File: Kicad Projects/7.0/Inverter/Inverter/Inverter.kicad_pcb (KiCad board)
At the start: 4 copper layers, 80.3 x 134.5 mm, 107 parts, among them IC1 1ED3322MC12NXUMA1, IC2 B0505S-2W, IC3 B0505S-2W, IC4 B0505S-2W, IC5 1ED3322MC12NXUMA1, J1 Conn_01x02_Male, J2 Conn_01x07_Male, J3 Conn_01x02_Male, J4 Output Selector, J5 Conn_01x07_Male, J6 Conn_01x03_Pin, J7 Conn_01x03_Pin, Q1 FS8205, Q2 FS8205, U1 LM7809_TO220, U2 LM7809_TO220, U3 LM7809_TO220, U4 AMS1117-5.0, U5 AMS1117-5.0, U6 AMS1117-5.0, U7 FF300R12KS4, U8 AMS1117-3.3, U9 ChinaBluePill

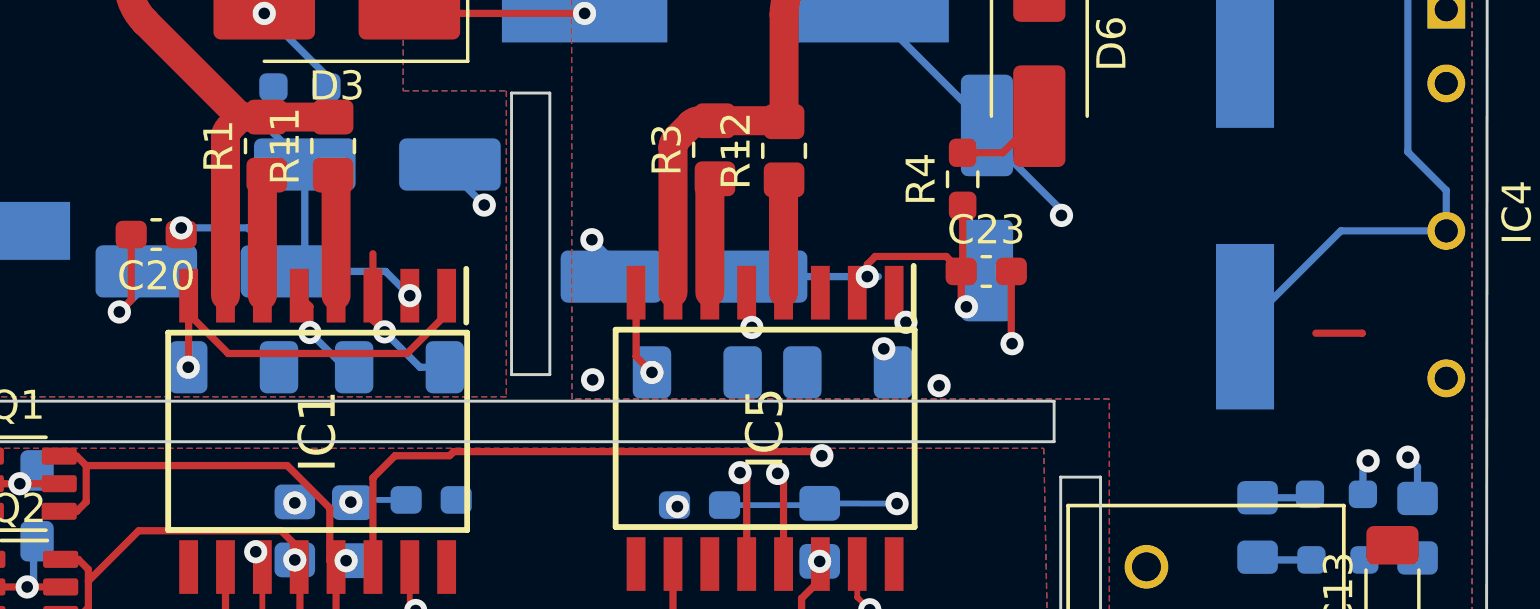
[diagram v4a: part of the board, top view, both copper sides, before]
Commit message: Inverter changes - power routing - incomplete
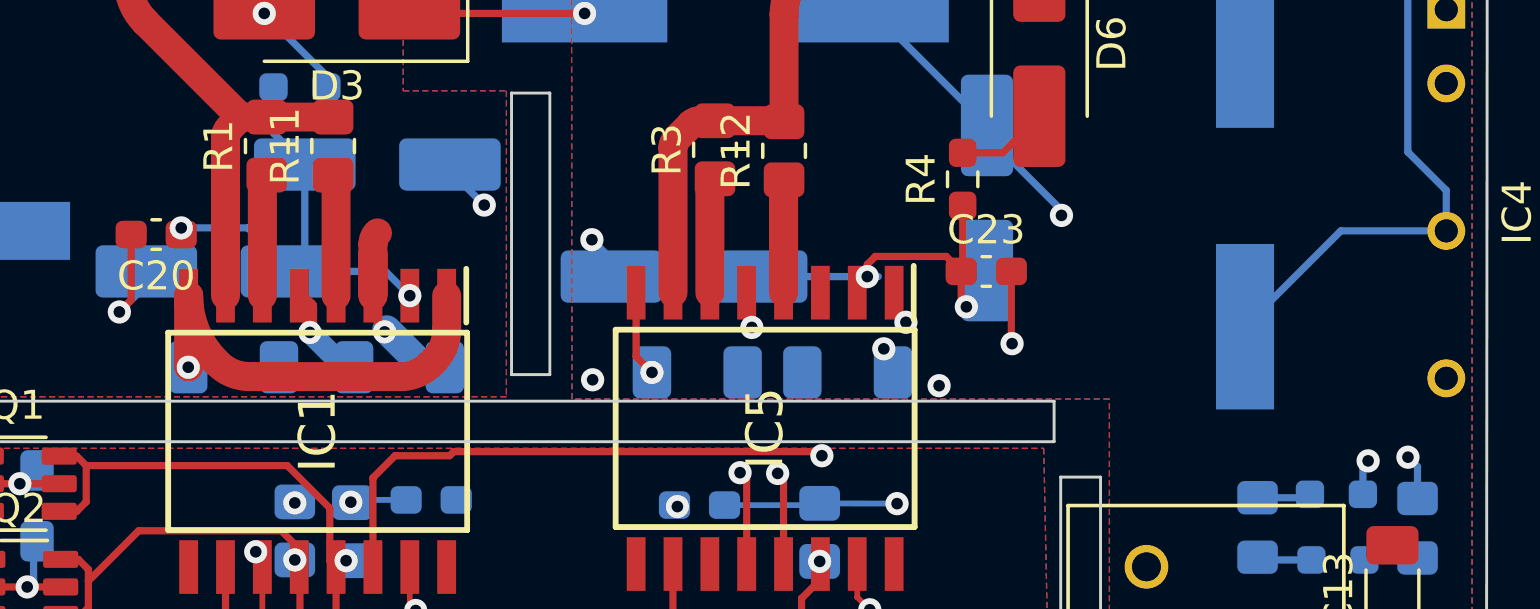
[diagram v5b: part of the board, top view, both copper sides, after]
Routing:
- net GND1: track 7.37 -> 11.9 mm
- net VDrive1Neg: track 23.4 -> 25.4 mm
- net GND2: track 11.4 -> 9.84 mm
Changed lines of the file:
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@@
   (segment (start 48.1584 155.9175) (end 50.9139 155.9175) (width 0.25) (layer "B.Cu") (net 5))
   (segment (start 25.908 130.302) (end 26.035 130.429) (width 0.25) (layer "F.Cu") (net 6))
-  (segment (start 52.920645 134.680445) (end 52.5526 134.3124) (width 0.25) (layer "F.Cu") (net 6))
+  (segment (start 52.920645 134.680445) (end 52.5526 134.3124) (width 0.5) (layer "F.Cu") (net 6))
   (segment (start 52.5526 134.3124) (end 52.5526 134.8871) (width 0.25) (layer "F.Cu") (net 6))
-  (segment (start 52.920645 135.580944) (end 52.920645 134.680445) (width 0.25) (layer "F.Cu") (net 6))
+  (segment (start 52.920645 135.580944) (end 52.920645 134.680445) (width 0.5) (layer "F.Cu") (net 6))
   (segment (start 23.622 130.302) (end 25.908 130.302) (width 0.25) (layer "F.Cu") (net 6))
   (segment (start 37.75588 135.03788) (end 37.973 135.255) (width 0.25) (layer "F.Cu") (net 6))
@@
   (via (at 37.973 135.255) (size 0.8) (drill 0.4) (layers "F.Cu" "B.Cu") (net 6))
   (via (at 26.035 130.429) (size 0.8) (drill 0.4) (layers "F.Cu" "B.Cu") (net 6))
-  (segment (start 54.118701 136.779) (end 52.920645 135.580944) (width 0.25) (layer "B.Cu") (net 6))
+  (segment (start 52.920645 135.580944) (end 54.118701 136.779) (width 0.75) (layer "B.Cu") (net 6))
   (segment (start 19.837 137.019) (end 19.587 137.019) (width 0.25) (layer "B.Cu") (net 6))
   (segment (start 18.2195 139.8955) (end 16.365 139.8955) (width 0.25) (layer "B.Cu") (net 6))
@@
   (segment (start 54.4445 136.779) (end 54.118701 136.779) (width 0.25) (layer "B.Cu") (net 6))
   (segment (start 35.7995 131.69) (end 35.9175 131.572) (width 0.25) (layer "F.Cu") (net 7))
-  (segment (start 55.0926 134.3124) (end 55.0926 132.8674) (width 0.25) (layer "F.Cu") (net 7))
-  (segment (start 55.0926 135.159102) (end 55.494201 135.560703) (width 0.25) (layer "F.Cu") (net 7))
+  (segment (start 55.0926 134.3124) (end 55.0926 132.8674) (width 1) (layer "F.Cu") (net 7))
+  (segment (start 55.0926 134.3124) (end 55.0926 132.529997) (width 1) (layer "F.Cu") (net 7))
+  (segment (start 55.0926 134.3124) (end 55.0926 134.591153) (width 0.25) (layer "F.Cu") (net 7))
   (segment (start 34.036 131.69) (end 35.7995 131.69) (width 0.25) (layer "F.Cu") (net 7))
-  (segment (start 55.0926 134.3124) (end 55.0926 135.159102) (width 0.25) (layer "F.Cu") (net 7))
   (via (at 55.494201 135.560703) (size 0.8) (drill 0.4) (layers "F.Cu" "B.Cu") (net 7))
-  (segment (start 56.712498 136.779) (end 57.5695 136.779) (width 0.25) (layer "B.Cu") (net 7))
-  (segment (start 55.494201 135.560703) (end 56.712498 136.779) (width 0.25) (layer "B.Cu") (net 7))
+  (arc (start 55.0926 134.591153) (mid 55.196972 135.115869) (end 55.494201 135.560703) (width 0.25) (layer "F.Cu") (net 7))
+  (arc (start 55.0926 132.529997) (mid 55.133507 132.324344) (end 55.25 132.15) (width 1) (layer "F.Cu") (net 7))
+  (segment (start 55.494201 135.560703) (end 56.106506 136.173008) (width 0.25) (layer "B.Cu") (net 7))
+  (segment (start 57.5695 136.779) (end 56.85743 136.779) (width 1) (layer "B.Cu") (net 7))
+  (segment (start 56.85743 136.779) (end 55.566667 135.488237) (width 1) (layer "B.Cu") (net 7))
+  (arc (start 56.106506 136.173008) (mid 56.777733 136.621508) (end 57.5695 136.779) (width 0.25) (layer "B.Cu") (net 7))
   (segment (start 90.1954 151.3463) (end 91.6309 151.3463) (width 0.25) (layer "F.Cu") (net 8))
   (segment (start 91.6309 151.3463) (end 91.9988 151.7142) (width 0.25) (layer "F.Cu") (net 8))
@@
   (segment (start 76.2254 128.778) (end 78.8162 131.3688) (width 0.25) (layer "B.Cu") (net 8))
   (segment (start 56.348 124.587) (end 62.3852 124.587) (width 0.25) (layer "F.Cu") (net 9))
-  (segment (start 87.5806 135.6062) (end 89.175 135.6062) (width 0.25) (layer "F.Cu") (net 9))
-  (segment (start 89.175 135.6062) (end 89.1794 135.6106) (width 0.25) (layer "F.Cu") (net 9))
   (via (at 62.6618 137.2108) (size 0.8) (drill 0.4) (layers "F.Cu" "B.Cu") (free) (net 9))
   (via (at 74.5998 137.414) (size 0.8) (drill 0.4) (layers "F.Cu" "B.Cu") (free) (net 9))
@@
   (segment (start 54.4068 141.351) (end 54.3306 141.4272) (width 0.2) (layer "B.Cu") (net 15))
   (segment (start 37.9749 140.589) (end 37.0586 140.589) (width 0.2) (layer "B.Cu") (net 15))
-  (segment (start 48.7426 134.3124) (end 48.7426 136.7659) (width 0.25) (layer "F.Cu") (net 16))
+  (segment (start 57.6326 135.505612) (end 57.6326 134.3124) (width 1) (layer "F.Cu") (net 16))
+  (segment (start 48.7426 134.3124) (end 48.7426 136.7659) (width 1) (layer "F.Cu") (net 16))
   (segment (start 46.7625 134.4665) (end 46.355 134.874) (width 0.25) (layer "F.Cu") (net 16))
   (segment (start 39.624 133.74) (end 39.624 135.128) (width 0.25) (layer "F.Cu") (net 16))
-  (segment (start 56.269056 136.305944) (end 50.106144 136.305944) (width 0.25) (layer "F.Cu") (net 16))
   (segment (start 39.624 135.128) (end 39.497 135.255) (width 0.25) (layer "F.Cu") (net 16))
+  (segment (start 49.683193 136.583194) (end 49.75 136.65) (width 0.25) (layer "F.Cu") (net 16))
   (segment (start 46.7625 132.207) (end 46.7625 134.4665) (width 0.25) (layer "F.Cu") (net 16))
   (segment (start 48.7426 134.9424) (end 48.7426 134.3124) (width 0.25) (layer "F.Cu") (net 16))
-  (segment (start 57.6326 134.3124) (end 57.6326 134.9424) (width 0.25) (layer "F.Cu") (net 16))
-  (segment (start 57.6326 134.9424) (end 56.269056 136.305944) (width 0.25) (layer "F.Cu") (net 16))
   (segment (start 48.7426 136.7659) (end 48.7295 136.779) (width 0.25) (layer "F.Cu") (net 16))
-  (segment (start 50.106144 136.305944) (end 48.7426 134.9424) (width 0.25) (layer "F.Cu") (net 16))
+  (segment (start 50.836396 137.1) (end 56.05 137.1) (width 1) (layer "F.Cu") (net 16))
+  (segment (start 57.074264 136.675736) (end 57.2 136.55) (width 1) (layer "F.Cu") (net 16))
   (via (at 46.355 134.874) (size 0.8) (drill 0.4) (layers "F.Cu" "B.Cu") (net 16))
   (via (at 31.877 125.476) (size 0.8) (drill 0.4) (layers "F.Cu" "B.Cu") (net 16))
@@
   (via (at 39.497 135.255) (size 0.8) (drill 0.4) (layers "F.Cu" "B.Cu") (net 16))
   (via (at 31.877 130.302) (size 0.8) (drill 0.4) (layers "F.Cu" "B.Cu") (net 16))
+  (arc (start 48.7426 134.3124) (mid 48.987052 135.541345) (end 49.683193 136.583194) (width 1) (layer "F.Cu") (net 16))
+  (arc (start 56.05 137.1) (mid 56.604328 136.989737) (end 57.074264 136.675736) (width 1) (layer "F.Cu") (net 16))
+  (arc (start 49.75 136.65) (mid 50.248442 136.983049) (end 50.836396 137.1) (width 1) (layer "F.Cu") (net 16))
+  (arc (start 57.2 136.55) (mid 57.520171 136.070831) (end 57.6326 135.505612) (width 1) (layer "F.Cu") (net 16))
   (segment (start 47.284 133.477) (end 47.284 133.945) (width 0.25) (layer "B.Cu") (net 16))
   (segment (start 31.623 123.9905) (end 31.623 125.222) (width 0.25) (layer "B.Cu") (net 16))

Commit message: Inverter gbr generated
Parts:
- removed H1, H2, H3, H4: MountingHole, MountingHole:MountingHole_3.2mm_M3
- added J10: Conn_01x02_Pin, Connector_PinHeader_1.27mm:PinHeader_1x02_P1.27mm_Vertical, F.Cu at (84.0, 99.2)
- added J11: Conn_01x02_Pin, Connector_PinHeader_1.27mm:PinHeader_1x02_P1.27mm_Vertical, F.Cu at (87.5, 35.9)
- added J8: Conn_01x02_Pin, Connector_PinHeader_1.27mm:PinHeader_1x02_P1.27mm_Vertical, F.Cu at (88.4, 78.5)
- added J9: NTC, Connector_PinHeader_1.27mm:PinHeader_1x02_P1.27mm_Vertical, F.Cu at (49.0, 151.2)
- added R28: NTC Complement, Resistor_SMD:R_0805_2012Metric_Pad1.20x1.40mm_HandSolder, F.Cu at (49.6, 148.5)
- J2, J5: footprint Connector_JST:JST_XH_B7B-XH-A_1x07_P2.50mm_Vertical -> Connector_JST:JST_XH_B8B-XH-A_1x08_P2.50mm_Vertical
- moved J7 0.55 mm to (86.3, 31.8)
- moved J6 0.55 mm to (81.5, 107.8)
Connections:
- J6 pad 2: Net-(J6-Pin_2) -> Net-(J10-Pin_2)
- J7 pad 2: Net-(J6-Pin_2) -> Net-(J11-Pin_1)
- U9 pad PA0: unconnected-(U9-PadPA0) -> Net-(J8-Pin_1)
- U9 pad PA1: unconnected-(U9-PadPA1) -> Net-(J5-Pin_8)
- U9 pad PA12: Net-(J6-Pin_2) -> Net-(J10-Pin_1)
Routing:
- net Net-(J6-Pin_2): track 91.6 -> 0.00 mm, vias 1 -> 0
- net Net-(J10-Pin_1): track 0.00 -> 79.7 mm, vias 0 -> 1
- net /3V3 MCU: track 19.1 -> 65.6 mm, vias 4 -> 8
- net Net-(J5-Pin_8): track 0.00 -> 29.2 mm
- net Net-(J2-Pin_8): track 0.00 -> 28.3 mm
- net VDrive2Neg: track 31.2 -> 51.7 mm, vias 5 -> 6
- net GND2: track 9.84 -> 25.8 mm, vias 3 -> 4
- net GND1: track 11.9 -> 24.4 mm, vias 1 -> 2
- net Net-(J10-Pin_2): track 0.00 -> 7.28 mm
- net Net-(J11-Pin_1): track 0.00 -> 6.90 mm
- net VDrive2: track 17.1 -> 23.1 mm, vias 6 -> 8
- net Net-(IC5-CLAMP): track 20.2 -> 25.9 mm
- net Net-(J8-Pin_1): track 0.00 -> 3.51 mm
- net /OUTHS: track 0.00 -> 2.81 mm
- net INLS: track 33.3 -> 35.7 mm
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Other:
- outline, holes or cut-outs redrawn
- board text added: "NTC"

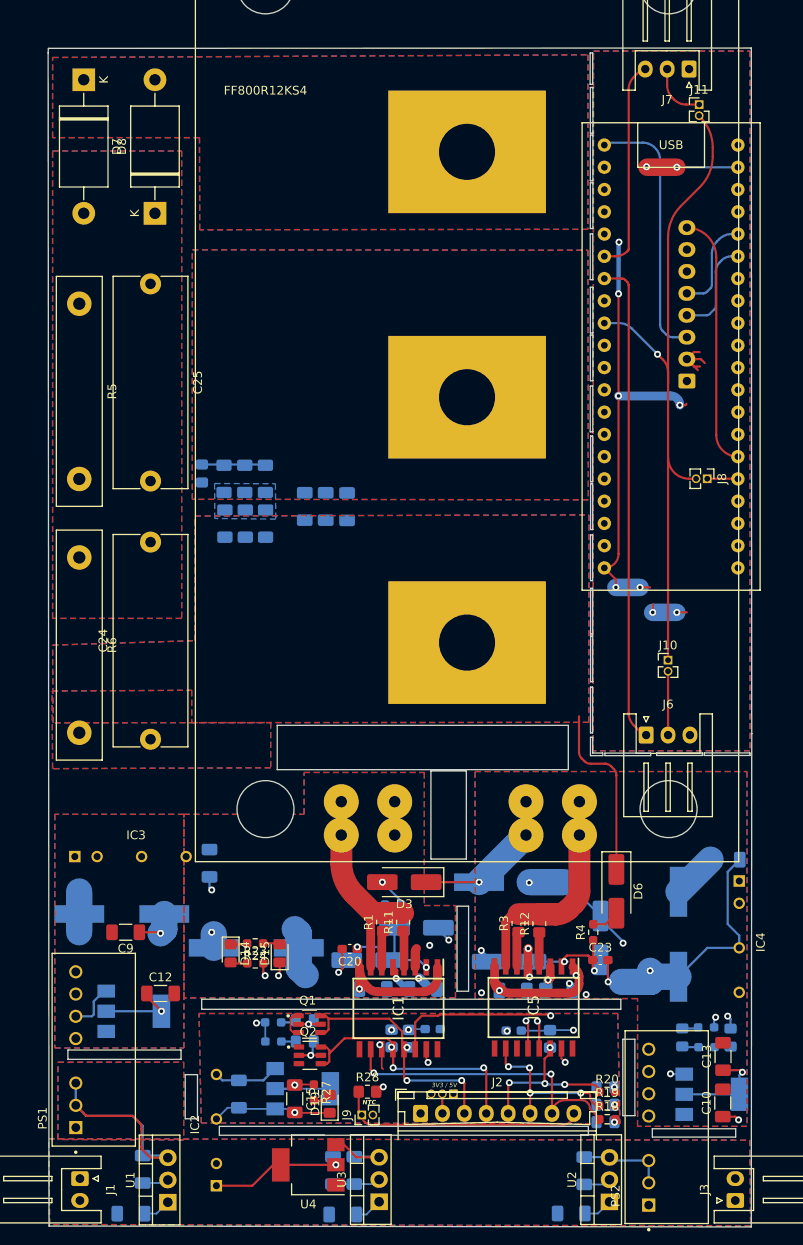
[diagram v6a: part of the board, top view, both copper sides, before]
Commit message: Inverter add dc link sense
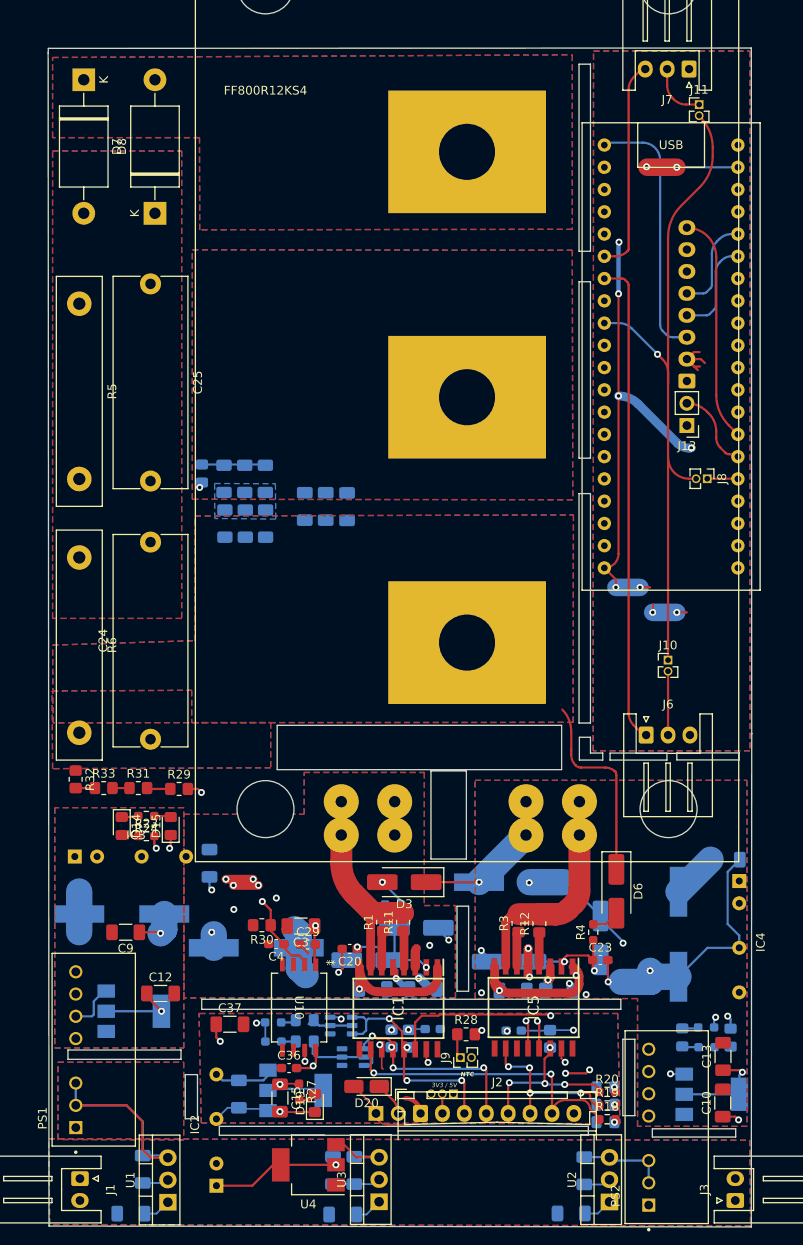
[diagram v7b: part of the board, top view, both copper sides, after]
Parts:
- added C29: 100nF, Capacitor_SMD:C_0603_1608Metric_Pad1.08x0.95mm_HandSolder, F.Cu at (42.9, 131.7)
- added C3: 1uF, Capacitor_SMD:C_1206_3216Metric_Pad1.33x1.80mm_HandSolder, F.Cu at (42.0, 129.6)
- added C36: 100nF, Capacitor_SMD:C_0603_1608Metric_Pad1.08x0.95mm_HandSolder, F.Cu at (40.7, 145.8)
- added C37: 1uF, Capacitor_SMD:C_1206_3216Metric_Pad1.33x1.80mm_HandSolder, F.Cu at (34.0, 140.8)
- added C4: 100nF, Capacitor_SMD:C_0603_1608Metric_Pad1.08x0.95mm_HandSolder, F.Cu at (39.2, 131.7)
- added D20: 3.3V zener, Diode_SMD:D_MicroMELF_Handsoldering, F.Cu at (49.5, 147.9)
- added J12: DC Link Sense, Connector_PinHeader_2.54mm:PinHeader_1x02_P2.54mm_Vertical, B.Cu at (50.6, 151.0)
- added J13: DC Link Sense, Connector_PinHeader_2.54mm:PinHeader_1x02_P2.54mm_Vertical, F.Cu at (86.1, 72.5)
- added R29: 22K, Resistor_SMD:R_0805_2012Metric_Pad1.20x1.40mm_HandSolder, F.Cu at (28.1, 114.0)
- added R30: 1K, Resistor_SMD:R_0805_2012Metric_Pad1.20x1.40mm_HandSolder, F.Cu at (37.6, 129.5)
- added R31: 22k, Resistor_SMD:R_0805_2012Metric_Pad1.20x1.40mm_HandSolder, F.Cu at (23.5, 113.8)
- added R32: 22k, Resistor_SMD:R_0805_2012Metric_Pad1.20x1.40mm_HandSolder, F.Cu at (16.4, 112.8)
- added R33: 22K, Resistor_SMD:R_0805_2012Metric_Pad1.20x1.40mm_HandSolder, F.Cu at (19.6, 113.8)
- added U10: ADUM4195-1BRIZ, ADUM4195-1:RI-8-1_ADI, F.Cu at (41.9, 138.9)
- Q1, Q2: moved to B.Cu
- moved D14 19.1 mm to (21.6, 118.2)
- moved D15 19.1 mm to (27.2, 118.2)
- moved R23 19.1 mm to (24.4, 119.3)
- moved R24 19.1 mm to (24.4, 117.0)
- moved J9 13.0 mm to (60.2, 144.6)
- moved R28 13.0 mm to (60.9, 141.9)
- moved Q2 4.93 mm to (48.0, 144.6)
- moved Q1 3.62 mm to (46.6, 140.9)
- moved C15 1.69 mm to (39.7, 149.2)
- moved D19 1.69 mm to (43.6, 149.8)
- moved R27 1.69 mm to (41.8, 148.5)
- moved U8 0.84 mm to (41.5, 148.3)
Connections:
- net Net-(U5-VO) renamed VDrive1_5V
- U9 pad PA1: Net-(J5-Pin_8) -> Net-(J13-Pin_2)
- U9 pad PA2: unconnected-(U9-PadPA2) -> Net-(J5-Pin_8)
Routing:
- net VDrive1_5V: track 33.2 -> 64.1 mm, vias 1 -> 2
- net Net-(U10-VIN): track 0.00 -> 26.8 mm, vias 0 -> 2
- net Net-(D20-K): track 0.00 -> 19.7 mm, vias 0 -> 1
- net /3V3 MCU: track 65.6 -> 78.6 mm
- net DIG-: track 26.0 -> 36.5 mm, vias 3 -> 4
- net Net-(J13-Pin_2): track 0.00 -> 9.41 mm
- net DIG5V: track 8.85 -> 18.1 mm, vias 0 -> 4
- net VDrive1: track 17.8 -> 25.5 mm, vias 4 -> 8
- net Net-(J2-Pin_8): track 28.3 -> 23.4 mm
- net RDY: track 52.1 -> 47.7 mm, vias 4 -> 5
- net FLT: track 50.2 -> 46.3 mm, vias 4 -> 5
- net Net-(D13-K): track 3.74 -> 6.95 mm, vias 1 -> 0
- net Net-(J5-Pin_8): track 29.2 -> 26.2 mm
- net Net-(R29-Pad1): track 0.00 -> 2.69 mm
- net +BATT: track 20.8 -> 23.2 mm
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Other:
- outline, holes or cut-outs redrawn
